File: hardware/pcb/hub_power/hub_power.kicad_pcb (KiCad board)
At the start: 2 copper layers, 44 x 81.2 mm, 58 parts, among them J1 XIAO D0-D6, J10 BAT (JST-PH), J13 USB-C, J14 XIAO PWR, J2 OLED, J4 SPK IN, J5 SPK OUT, J6 REED+BTN2, K31 G6S-2F DC5, Q1 MMUN2133LT1G, Q31 SS8050, SW1 MST-12D18G3, U1 TPS61090RSAR, U2 MCP73871-2CCI/ML, U3 INA226AIDGSR, U4 AS5600-ASOM

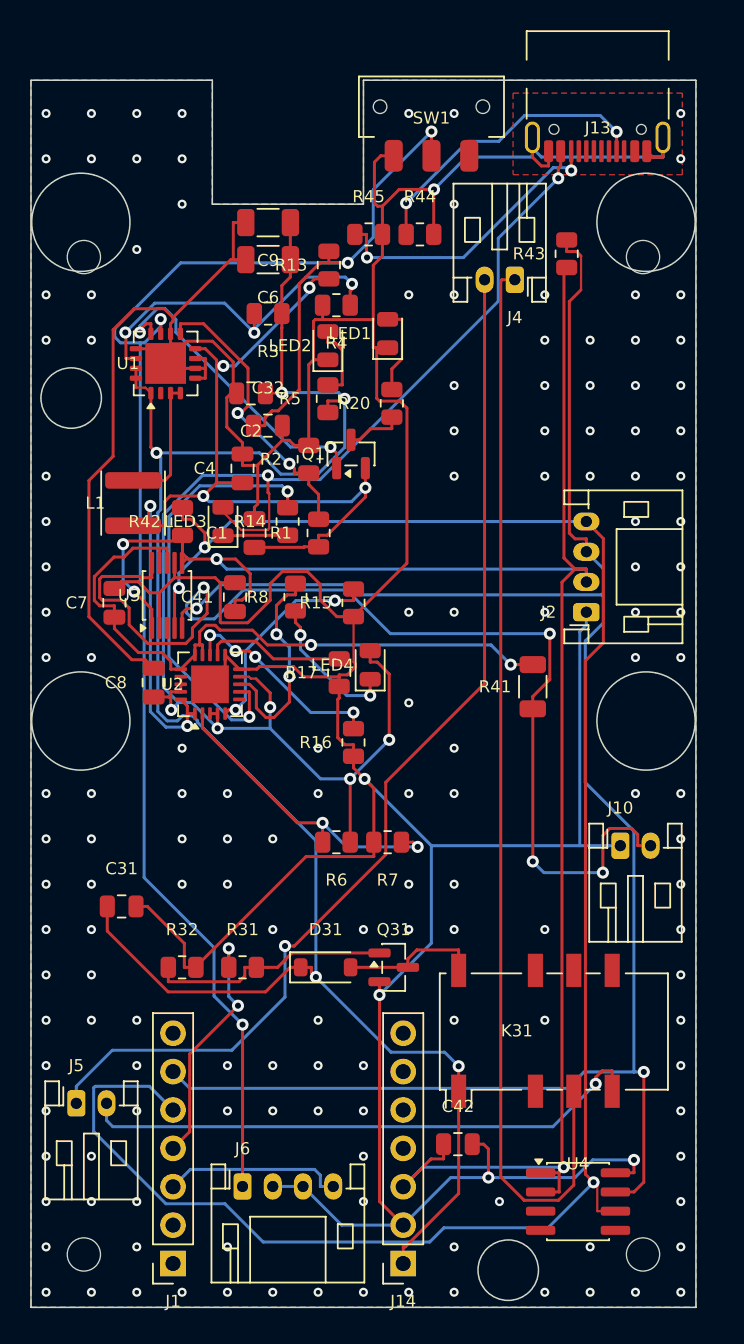
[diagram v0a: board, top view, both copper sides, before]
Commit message: 🔴 取付穴の上 2 つを下げる — 柱との芯間 2.309 でねじが入らなかった
ユーザーが模型を拡大して「これにどうやってネジいれるんですか？」。数えたら、
ハブの上の取付穴（3.5 / 40.5, 69.5）と OLED の柱（3.30 / 40.70, 71.80）の芯間が 2.309 で、
- 通し穴 φ2.6 と φ2.2 は半径の和 2.40 ⇒ 0.09 重なって 1 つの長穴になる
- ザグリ φ4 どうしは 1.69 重なる
- M2 のなべ頭 φ3.8 とナット（二面幅 4.0）は並ばない

- 🔒 上の 2 穴を Y 69.5 → **65.25** へ（柱まで 6.55）。格子 37 × 66 → **37 × 61.75**。
  左右そろう位置を板の全面から総当たりで探して選んだ（X 3.5 の列は柱 2 本に挟まれて
  Y 65.25 / 78.25 / 78.5 の 3 か所しか無い）
- J4（スピーカー IN）を 1.5mm 上げて場所を空けた
- ⛔ 「上の 2 本をやめて 2 点留めにする」案は断った。残る 2 点はどちらも板 Y 3.5 で
  同じ縁に並び、板がその線を軸に回る。ReSpeaker を真上から押し込む板なので保たない
- 🔴 **取付穴どうし・取付穴と柱の芯間の検査**を足した。枠の重なりだけ見ていて、
  ねじを回す物どうしの間隔を見ていなかった（口の通り道と同じ形の見落とし）
- 縫うビアの格子を 3.0 → 3.2 に（GND のベタの島が 1 つ孤立していた。111 個へ）
- POWER.md: 共締てを落とした理由を「不要だから」→「芯間を誰も数えていなかったから」に直した

結果: 配線 714 本 ＋ 縫うビア 111 個・未配線 0・DRC エラー 0・
check_sch 0 件・check_pcb は下限 0.15mm に対していちばん近いのが 0.152mm・
ねじの間隔 ✅・ナットの下 ✅・プラグの通り道 5 口 ✅・パッドの検算 4 点一致。
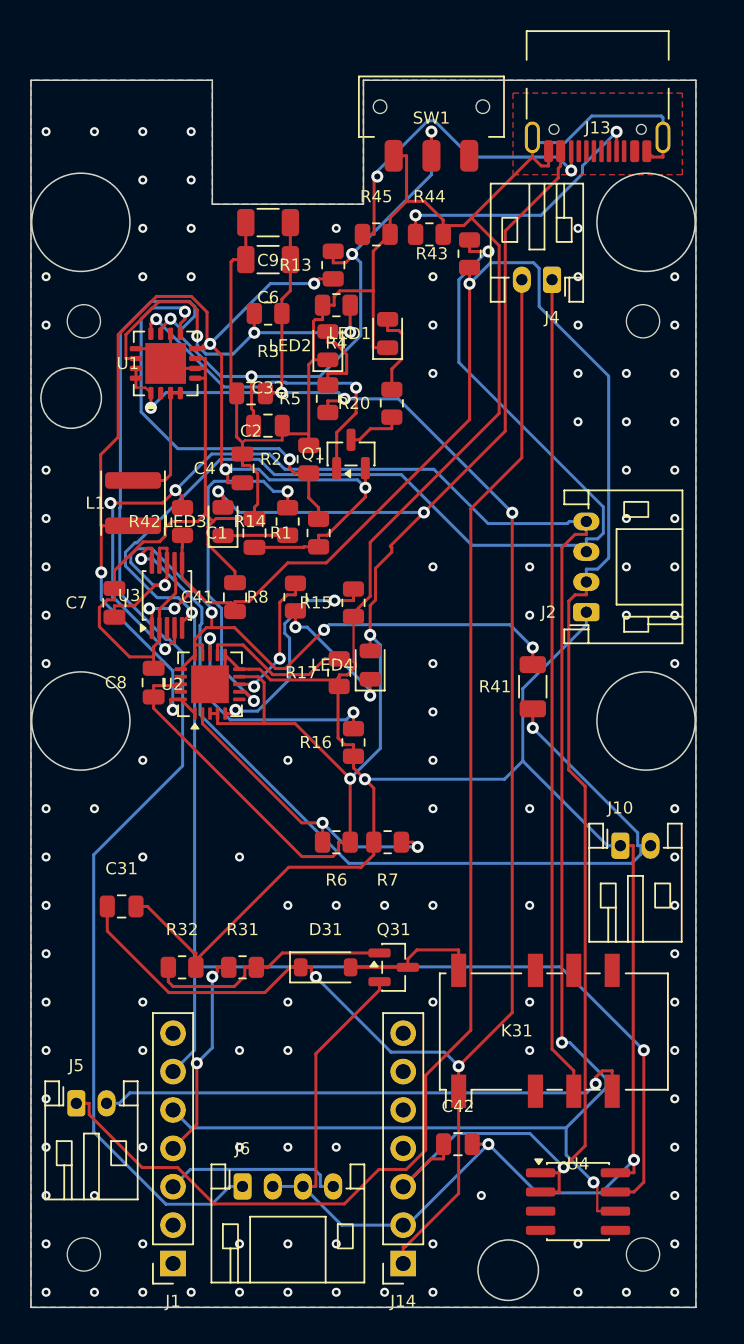
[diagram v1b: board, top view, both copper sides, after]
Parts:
- moved R43 6.43 mm to (89.0, 51.5)
- moved ? 4.25 mm to (63.5, 56.0)
- moved ? 4.25 mm to (100.5, 56.0)
- moved J4 2.47 mm to (94.5, 53.2)
- moved R44 0.63 mm to (86.4, 50.2)
- moved R45 0.51 mm to (82.8, 50.2)
- moved R13 0.29 mm to (80.0, 52.2)
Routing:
- net SPKP: track 72.4 -> 54.3 mm
- net SPKM: track 70.7 -> 88.0 mm, vias 1 -> 0
- net SCL: track 130.7 -> 144.8 mm, vias 2 -> 3
- net VSYS: track 72.0 -> 84.6 mm
- net BATP: track 73.3 -> 61.5 mm, vias 4 -> 2
- net LBI: track 19.6 -> 27.5 mm
- net VBUS: track 99.1 -> 106.6 mm, vias 7 -> 4
- net EN: track 110.0 -> 117.3 mm
- net V33: track 127.5 -> 134.5 mm
- net GND: track 327.5 -> 321.1 mm, vias 153 -> 114
- net VLIPO: track 45.2 -> 50.8 mm, vias 2 -> 4
- net STAT2: track 28.7 -> 23.4 mm
- net STAT1: track 14.4 -> 9.33 mm
- net SDA: track 130.4 -> 127.0 mm, vias 3 -> 5
- net IN: track 16.5 -> 14.0 mm
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
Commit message: 口の向きを表で持つのをやめ、置いてある足形から測る（手書きの OPEN_DIR は全部 180° 逆だった）
🔴 プラグの通り道の検査は 5 口とも「口の裏側」を見ていた。「5 口すべて空いている」は
裏側が空いていたという意味しか無く、実際は

  J2  相手が板の右の縁を 2.60 越えて殻の壁を貫く
  J4  相手が SW1 と J13 にぶつかる

という状態だった。ユーザーの「J4J5どうやって挿すんだ」への直しが、直し自体は
逆向きだったことになる。

直したもの:
- OPEN_DIR を捨て、open_dir() が**パッドの重心と枠の中心のずれ**から測る
  （口は必ずパッドと反対側に開く。📄 ePH.pdf 3 ページの足の位置が根拠）
- 帯の作り方を plug_band() 1 か所に閉じた（同じ式を 3 か所に書いて 2 か所で
  Y の符号を逆にしていた）
- J2 90°→270°・J4 180°→0°・J10 0°→180°。**どれもコメントに書いてあった意図の通りの向き**
  で、角度だけが壊れた表から出ていた。枠が動かないよう置き点も同じだけ動かした
- J2 は 270° にするとパッドが枠の反対の端へ移り、柱 (40.70, 38.80) の抜きに SCL と SDA が
  乗った。+3.3 上げた。**パッドと穴のすきまの検査**を新設（枠は柱を避けてもパッドは避けない）
- 口 5 つを FIXED に入れた。押し離しが口を動かすと通り道だけ取り残される
- 押し離しが押すのは相手の胴 3.1 まで。指のぶんまで押すと発散した
- 板の縁を越える帯は「間違い」ではなく「殻への注文」として別に出す
- C31/R32/R31 を Y 22.5 → 26.5。それまで車線が空いていたのは**向きを間違えた J5 の
  通り道**が C31 を押していたからで、直したら車線が消えて SCL が降りられなくなった

配線 732・縫いビア 101・未配線 0・DRC エラー 0・最小すきま 0.151mm・check_sch 0 件。
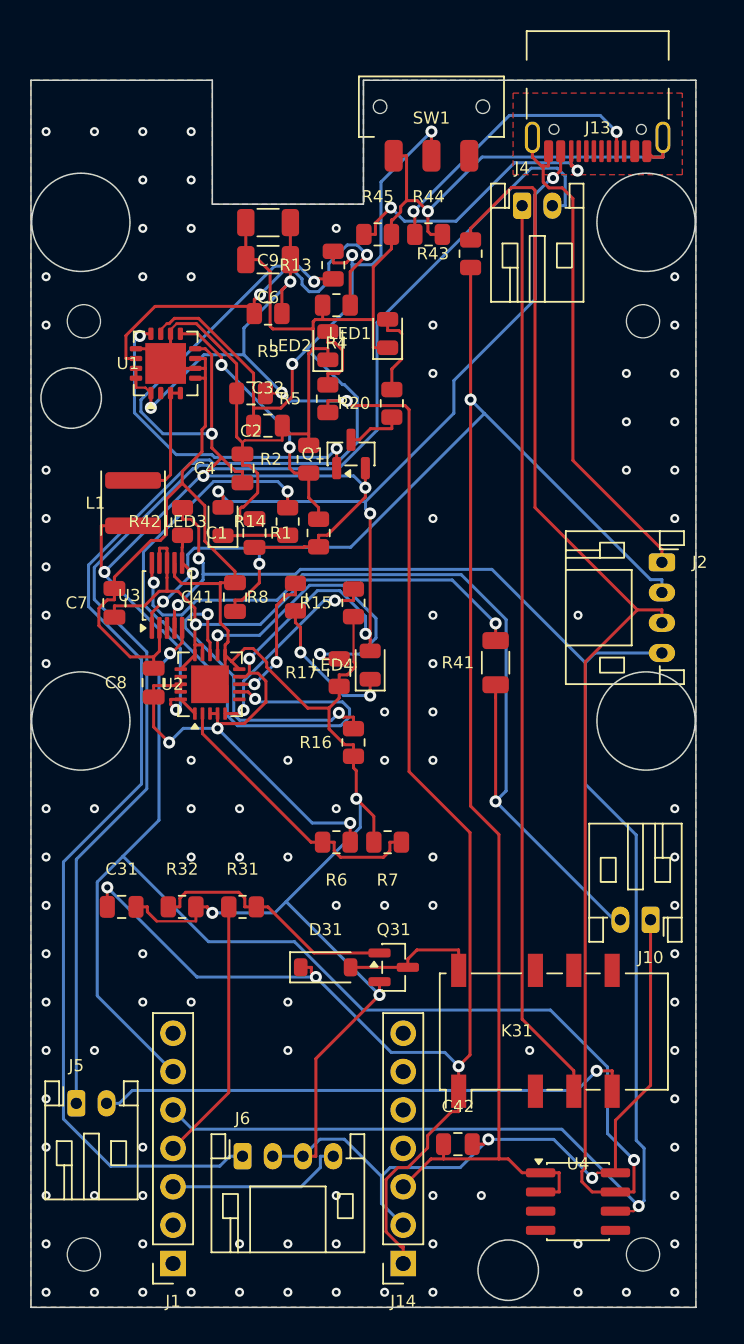
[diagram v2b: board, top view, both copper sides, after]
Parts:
- moved J2 5.99 mm to (101.8, 71.9), turned to 270 degrees
- moved J10 5.29 mm to (101.0, 95.5), turned to 180 degrees
- moved J4 5.29 mm to (92.5, 48.3), turned to 0 degrees
- moved R31 4.00 mm to (74.0, 94.7)
- moved R32 4.00 mm to (70.0, 94.7)
- moved R41 2.93 mm to (90.7, 78.5)
- moved J6 2.00 mm to (74.0, 111.2)
- moved R45 0.09 mm to (82.9, 50.2)
- moved R43 0.07 mm to (89.1, 51.5)
- moved R44 0.05 mm to (86.3, 50.2)
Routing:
- net STAT2: track 23.4 -> 42.9 mm
- net SCL: track 144.8 -> 163.0 mm, vias 3 -> 2
- net GND: track 321.1 -> 303.2 mm, vias 114 -> 107
- net VBUS: track 106.6 -> 94.4 mm, vias 4 -> 8
- net SDA: track 127.0 -> 115.8 mm, vias 5 -> 3
- net PROG3: track 9.96 -> 20.9 mm, vias 0 -> 2
- net VLIPO: track 50.8 -> 40.3 mm, vias 4 -> 2
- net LBI: track 27.5 -> 17.3 mm
- net EN: track 117.3 -> 123.9 mm, vias 4 -> 3
- net SPKP: track 54.3 -> 60.0 mm
- net PROG1: track 16.5 -> 21.1 mm
- net V33: track 134.5 -> 130.8 mm
- net IN: track 14.0 -> 17.5 mm, vias 2 -> 0
- net V5: track 128.4 -> 131.5 mm, vias 6 -> 7
- net FB: track 24.5 -> 27.5 mm, vias 3 -> 2
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
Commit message: J6 を 180° 回して口を谷（+Y）へ向ける — 殻を彫る話も上げる話も消える
調停役: 「線が壁へ向かって出ても曲げる場所が無い」（φ1.0 の線の曲げ半径は 5 倍で
5mm 見当・壁までは 2.25）。⇒ 口を板の内側へ向け、Y も元へ戻した。

  枠 板 X 11.55〜22.45 ・ Y 1.25〜9.85（箱 Y 4.25〜12.85）
  相手 3.1 も 指まで 10.0 も 谷の中で当たる物なし

⇒ 殻に空けてもらうのは J5 の下 3.25 だけになった。

未配線 0・DRC エラー 0・最小すきま 0.152mm。
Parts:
- moved J6 9.14 mm to (80.0, 118.1), turned to 180 degrees
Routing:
- net V5: track 131.5 -> 177.0 mm, vias 7 -> 5
- net GND: track 303.2 -> 346.8 mm, vias 107 -> 94
- net VBUS: track 94.4 -> 115.8 mm, vias 8 -> 5
- net V33: track 130.8 -> 150.4 mm
- net SCL: track 163.0 -> 143.4 mm, vias 2 -> 3
- net VSYS: track 86.3 -> 75.5 mm, vias 6 -> 5
- net EN: track 123.9 -> 114.3 mm
- net PROG3: track 20.9 -> 28.5 mm
- net FB: track 27.5 -> 21.1 mm
- net PROG1: track 21.1 -> 15.6 mm
- net BTN: track 11.9 -> 7.28 mm
- net BATP: track 60.4 -> 64.8 mm
- net CC2: track 19.0 -> 22.6 mm, vias 2 -> 0
- net LBO: track 22.2 -> 18.7 mm, vias 2 -> 0
- net SDA: track 115.8 -> 118.7 mm
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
